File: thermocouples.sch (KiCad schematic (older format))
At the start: 30 parts, among them J1 Screw_Terminal_01x10, J2 Screw_Terminal_01x10, U1 LTC2984CLX-DNP

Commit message: completed design 2.0
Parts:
- U1: footprint footprints:LTC2418IGN-PBF -> footprints:LTC2984CLX-PBF
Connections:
- net GND: now also J1.10 (Pin_10), J1.2 (Pin_2), J1.4 (Pin_4), J1.6 (Pin_6), J1.8 (Pin_8), J2.10 (Pin_10), J2.2 (Pin_2), J2.4 (Pin_4), J2.6 (Pin_6), J2.8 (Pin_8); no longer J1.1 (Pin_1), J1.3 (Pin_3), J1.5 (Pin_5), J1.7 (Pin_7), J1.9 (Pin_9), J2.1 (Pin_1), J2.3 (Pin_3), J2.5 (Pin_5), J2.7 (Pin_7), J2.9 (Pin_9)
- net TC5RAW: now reaches R10.1
- net TC5RAW: now also J2.9 (Pin_9); no longer J2.2 (Pin_2)
- net TC6RAW: now reaches R9.1
- net TC6RAW: now also J2.7 (Pin_7); no longer J2.4 (Pin_4)
- net TC7RAW: now reaches R8.1
- net TC7RAW: now also J2.5 (Pin_5); no longer J2.6 (Pin_6)
- net TC8RAW: now reaches R7.1
- net TC8RAW: now also J2.3 (Pin_3); no longer J2.8 (Pin_8)
- net TC9RAW: now reaches R6.1
- net TC9RAW: now also J2.1 (Pin_1); no longer J2.10 (Pin_10)
- net TC0RAW: now reaches R5.1
- net TC0RAW: now also J1.9 (Pin_9); no longer J1.2 (Pin_2)
- net TC1RAW: now reaches R4.1
- net TC1RAW: now also J1.7 (Pin_7); no longer J1.4 (Pin_4)
- net TC2RAW: now reaches R3.1
- net TC2RAW: now also J1.5 (Pin_5); no longer J1.6 (Pin_6)
- net TC3RAQ: now reaches R2.1
- net TC3RAQ: now also J1.3 (Pin_3); no longer J1.8 (Pin_8)
- net TC4RAW: now reaches R1.1
- net TC4RAW: now also J1.1 (Pin_1); no longer J1.10 (Pin_10)
- net at U1.16 (CH1): no longer D1.2 (A)
- net CJ: now reaches U1.27 (CH12)
- net CJ: now also D1.2 (A)
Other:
- moved on the sheet: D1
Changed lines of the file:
@@
 $EndComp
-Wire Wire Line
-	3550 3200 3550 3300
-Wire Wire Line
-	3550 3200 4200 3200
 Wire Wire Line
 	3350 2900 3350 3000
 Wire Wire Line
 	3350 2900 4050 2900
-Text GLabel 4200 3600 0    50   Input ~ 0
-TC0+
-Text GLabel 4200 3700 0    50   Input ~ 0
-TC1+
-Text GLabel 4200 3800 0    50   Input ~ 0
-TC2+
-Text GLabel 4200 3900 0    50   Input ~ 0
-TC3+
-Text GLabel 4200 4000 0    50   Input ~ 0
-TC4+
 Text GLabel 7400 3400 2    50   Input ~ 0
 TC5+
@@
 L Connector:Screw_Terminal_01x10 J1
 U 1 1 5EE8305E
-P 5000 5600
-F 0 "J1" H 5080 5592 50  0000 L CNN
-F 1 "Screw_Terminal_01x10" H 5080 5501 50  0000 L CNN
-F 2 "TerminalBlock_Phoenix:TerminalBlock_Phoenix_MPT-0,5-10-2.54_1x10_P2.54mm_Horizontal" H 5000 5600 50  0001 C CNN
-F 3 "~" H 5000 5600 50  0001 C CNN
-	1    5000 5600
-	1    0    0    1
+P 5000 5500
+F 0 "J1" H 5080 5492 50  0000 L CNN
+F 1 "Screw_Terminal_01x10" H 5080 5401 50  0000 L CNN
+F 2 "TerminalBlock_Phoenix:TerminalBlock_Phoenix_MPT-0,5-10-2.54_1x10_P2.54mm_Horizontal" H 5000 5500 50  0001 C CNN
+F 3 "~" H 5000 5500 50  0001 C CNN
+	1    5000 5500
+	1    0    0    -1
 $EndComp
 Wire Wire Line
@@
 L Diode:1N4148 D1
 U 1 1 5EE83070
-P 3550 3450
-F 0 "D1" V 3596 3371 50  0000 R CNN
-F 1 "1N4148" V 3505 3371 50  0000 R CNN
-F 2 "Diode_THT:D_DO-35_SOD27_P7.62mm_Horizontal" H 3550 3275 50  0001 C CNN
-F 3 "https://assets.nexperia.com/documents/data-sheet/1N4148_1N4448.pdf" H 3550 3450 50  0001 C CNN
-F 4 "DNP" H 3550 3450 50  0001 C CNN "place?"
-	1    3550 3450
-	0    -1   -1   0
+P 7750 3950
+F 0 "D1" V 7796 3871 50  0000 R CNN
+F 1 "1N4148" V 7705 3871 50  0000 R CNN
+F 2 "Diode_THT:D_DO-35_SOD27_P7.62mm_Horizontal" H 7750 3775 50  0001 C CNN
+F 3 "https://assets.nexperia.com/documents/data-sheet/1N4148_1N4448.pdf" H 7750 3950 50  0001 C CNN
+F 4 "DNP" H 7750 3950 50  0001 C CNN "place?"
+	1    7750 3950
+	0    1    -1   0
 $EndComp
 Text Notes 3300 4850 0    50   ~ 0
@@
 L Connector:Screw_Terminal_01x10 J2
 U 1 1 5EE83094
-P 7750 5600
-F 0 "J2" H 7830 5592 50  0000 L CNN
-F 1 "Screw_Terminal_01x10" H 7830 5501 50  0000 L CNN
-F 2 "TerminalBlock_Phoenix:TerminalBlock_Phoenix_MPT-0,5-10-2.54_1x10_P2.54mm_Horizontal" H 7750 5600 50  0001 C CNN
-F 3 "~" H 7750 5600 50  0001 C CNN
-	1    7750 5600
-	1    0    0    1
+P 7750 5500
+F 0 "J2" H 7830 5492 50  0000 L CNN
+F 1 "Screw_Terminal_01x10" H 7830 5401 50  0000 L CNN
+F 2 "TerminalBlock_Phoenix:TerminalBlock_Phoenix_MPT-0,5-10-2.54_1x10_P2.54mm_Horizontal" H 7750 5500 50  0001 C CNN
+F 3 "~" H 7750 5500 50  0001 C CNN
+	1    7750 5500
+	1    0    0    -1
 $EndComp
 Wire Wire Line
@@
 F 0 "U1" H 5800 2087 60  0000 C CNN
 F 1 "LTC2984CLX-DNP" H 5800 1981 60  0000 C CNN
-F 2 "footprints:LTC2418IGN-PBF" H 5800 1940 60  0001 C CNN
+F 2 "footprints:LTC2984CLX-PBF" H 5800 1940 60  0001 C CNN
 F 3 "" H 4200 1700 60  0000 C CNN
 F 4 "DNP" H 4200 1700 50  0001 C CNN "place?"
@@
 Text HLabel 3350 3300 0    50   Input ~ 0
 GND
-Text HLabel 3550 3600 0    50   Input ~ 0
+Text HLabel 7750 4100 2    50   Input ~ 0
 GND
 Text HLabel 8150 2350 2    50   Input ~ 0
@@
 Text HLabel 4200 3100 0    50   Input ~ 0
 GND
+Text Label 4800 5100 2    50   ~ 0
+TC4RAW
+Text Label 4800 5300 2    50   ~ 0
+TC3RAQ
+Text Label 4800 5500 2    50   ~ 0
+TC2RAW
+Text Label 4800 5700 2    50   ~ 0
+TC1RAW
+Text Label 4800 5900 2    50   ~ 0
+TC0RAW
+Text Label 7550 5100 2    50   ~ 0
+TC9RAW
+Text Label 7550 5300 2    50   ~ 0
+TC8RAW
+Text Label 7550 5500 2    50   ~ 0
+TC7RAW
+Text Label 7550 5700 2    50   ~ 0
+TC6RAW
+Text Label 7550 5900 2    50   ~ 0
+TC5RAW
+Text GLabel 4200 4000 0    50   Input ~ 0
+TC4+
+Text GLabel 4200 3900 0    50   Input ~ 0
+TC3+
+Text GLabel 4200 3800 0    50   Input ~ 0
+TC2+
+Text GLabel 4200 3700 0    50   Input ~ 0
+TC1+
+Text GLabel 4200 3600 0    50   Input ~ 0
+TC0+
+Wire Wire Line
+	7400 3800 7750 3800
+Text Label 7600 3800 2    50   ~ 0
+CJ
 $EndSCHEMATC

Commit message: added low pass filter to load cell inputs
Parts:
- D1: footprint Diode_THT:D_DO-35_SOD27_P7.62mm_Horizontal -> Diode_THT:D_A-405_P12.70mm_Horizontal
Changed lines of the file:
@@
 F 0 "D1" V 7796 3871 50  0000 R CNN
 F 1 "1N4148" V 7705 3871 50  0000 R CNN
-F 2 "Diode_THT:D_DO-35_SOD27_P7.62mm_Horizontal" H 7750 3775 50  0001 C CNN
+F 2 "Diode_THT:D_A-405_P12.70mm_Horizontal" H 7750 3775 50  0001 C CNN
 F 3 "https://assets.nexperia.com/documents/data-sheet/1N4148_1N4448.pdf" H 7750 3950 50  0001 C CNN
 F 4 "DNP" H 7750 3950 50  0001 C CNN "place?"

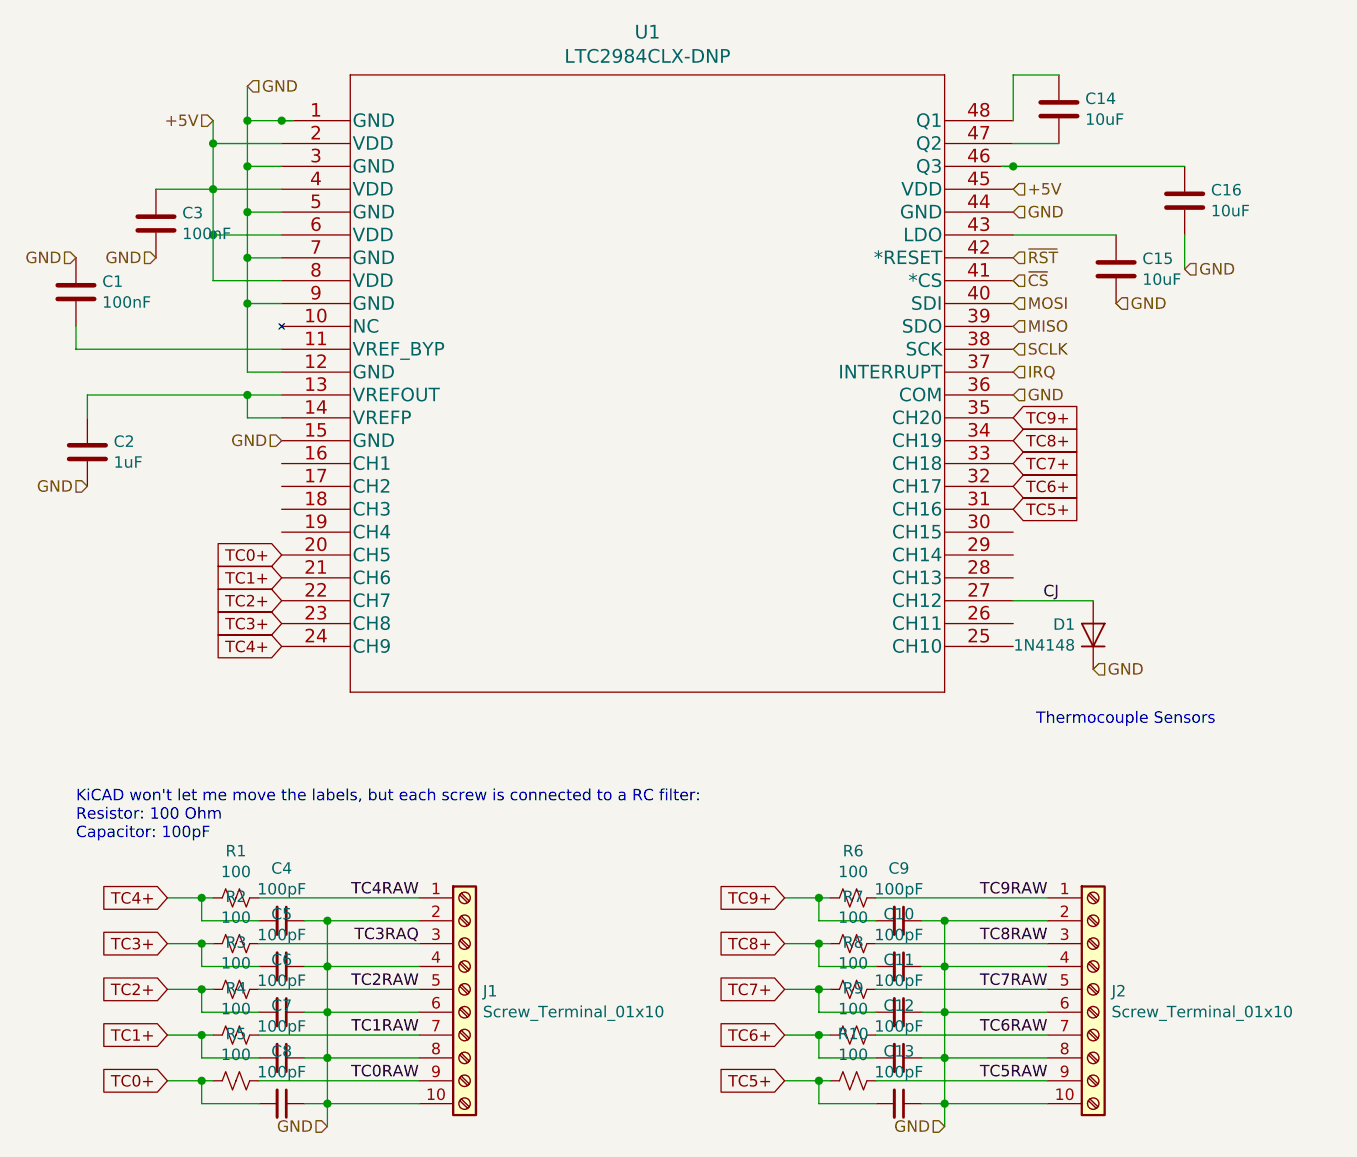
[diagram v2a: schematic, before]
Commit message: pcb size reduced to 3x3in
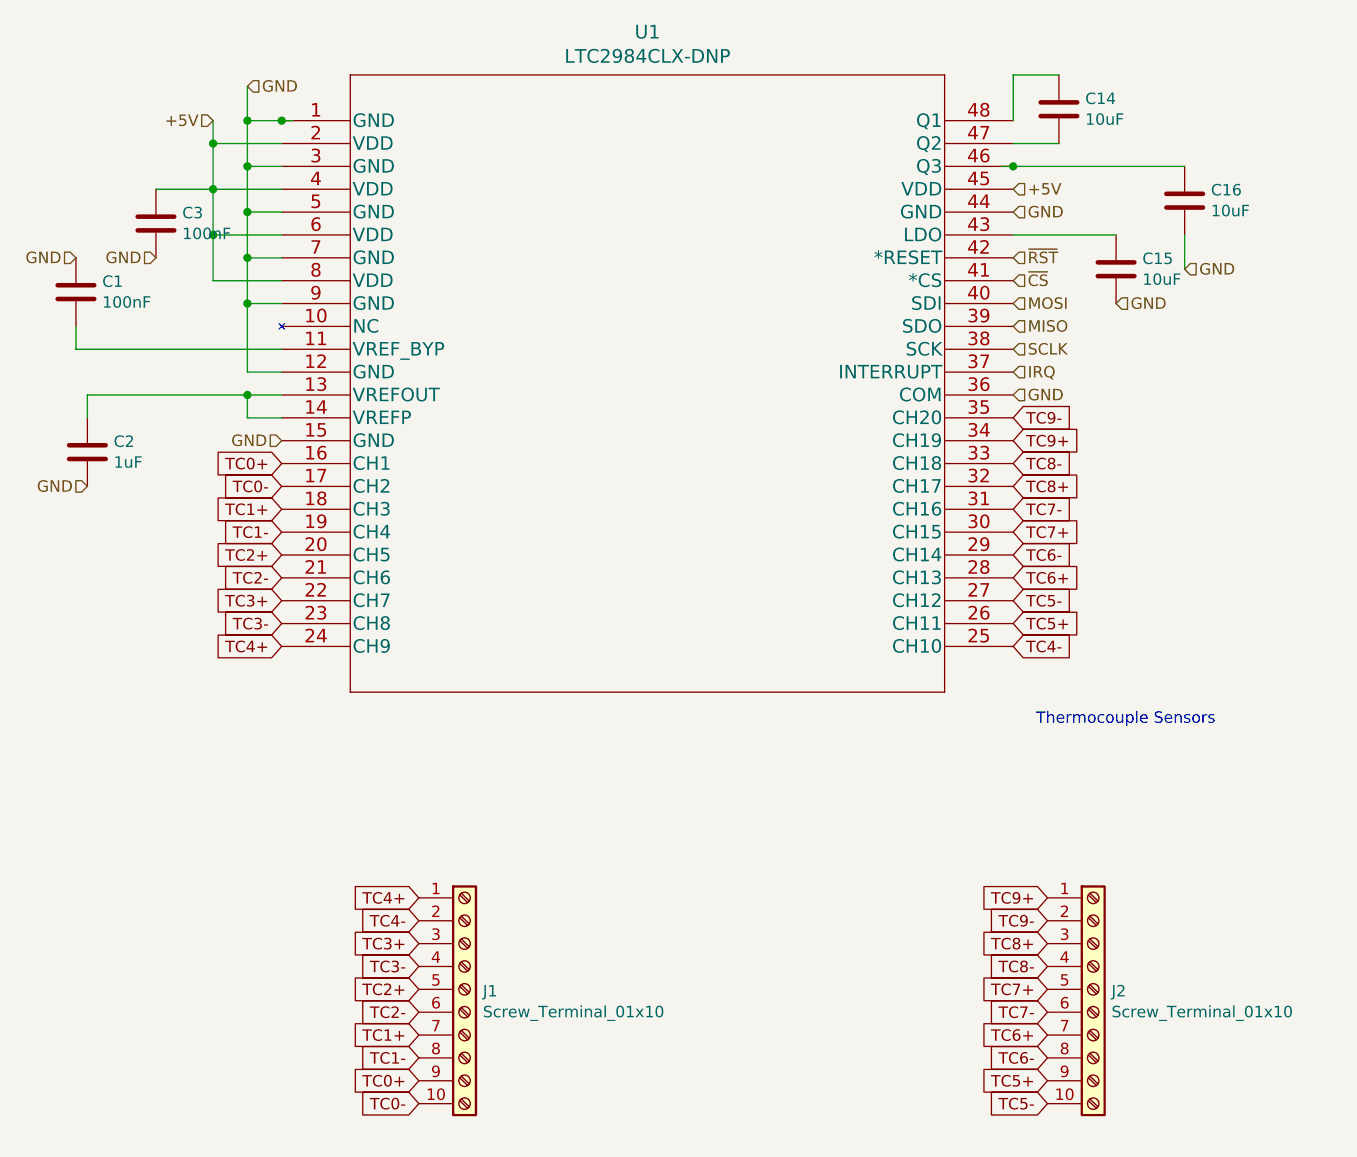
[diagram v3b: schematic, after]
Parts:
- removed C10, C11, C12, C13, C4, C5, C6, C7, C8, C9: 100pF, Capacitor_SMD:C_0805_2012Metric_Pad1.15x1.40mm_HandSolder, symbol Device:C_Small
- removed D1: 1N4148, Diode_THT:D_A-405_P12.70mm_Horizontal, symbol Diode:1N4148
- removed R1, R10, R2, R3, R4, R5, R6, R7, R8, R9: 100, Resistor_SMD:R_0805_2012Metric_Pad1.15x1.40mm_HandSolder, symbol Device:R_Small_US
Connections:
- net labels added: TC0-, TC1-, TC2-, TC3-, TC4-, TC5-, TC6-, TC7-, TC8-, TC9-
- net labels removed: CJ, TC0RAW, TC1RAW, TC2RAW, TC3RAQ, TC4RAW, TC5RAW, TC6RAW, TC7RAW, TC8RAW, TC9RAW
- wire segments 117 -> 36
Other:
- note removed: "KiCAD won't let me move the labels, but each screw is connected to a RC filter:\nResistor: 100 Ohm\nCapacitor: 100pF"
